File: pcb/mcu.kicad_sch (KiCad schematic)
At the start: 20 parts, among them J4 AVR-UPDI-6, U4 ATtiny1616-MNR

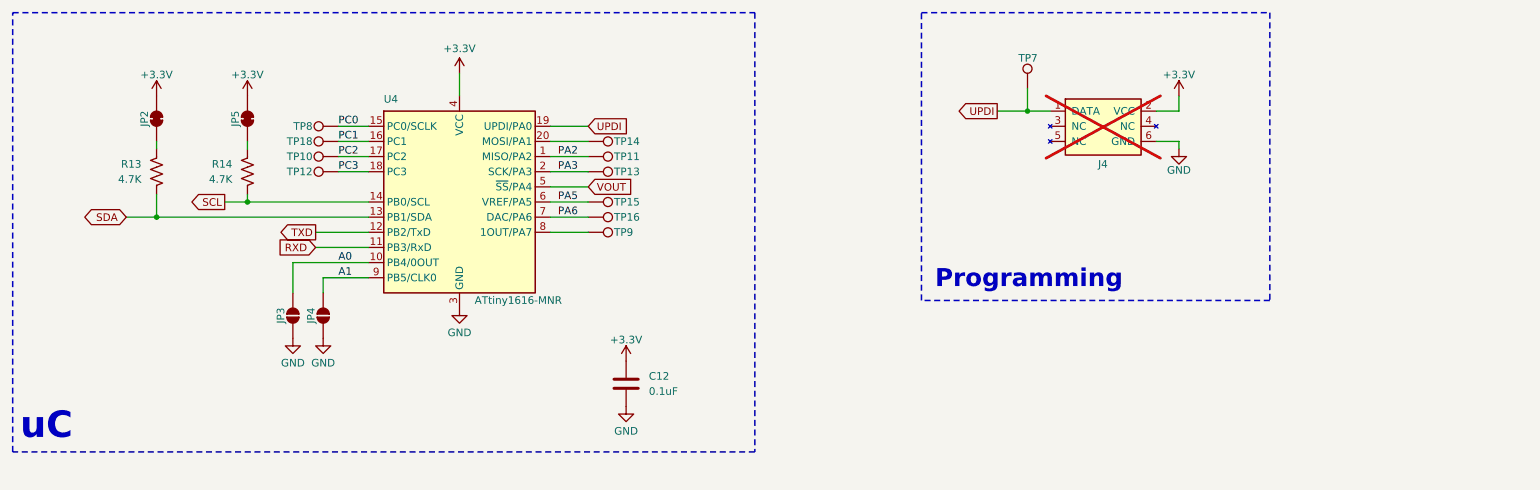
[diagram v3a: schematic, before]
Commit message: Updates for consistency
Changed mounting holes to grounded
Updated power connectors
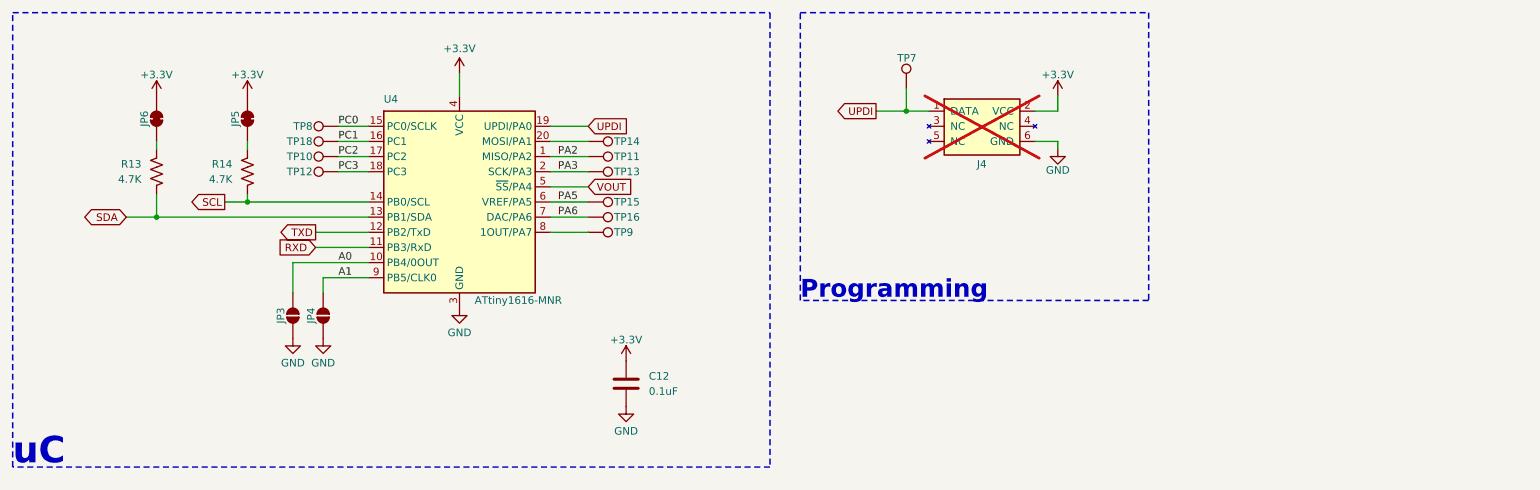
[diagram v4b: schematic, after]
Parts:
- renumbered JP2 to JP6
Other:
- moved on the sheet: J4, TP7
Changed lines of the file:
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@@
 	)
 	(rectangle
-		(start 177.8 25.4)
-		(end 236.22 73.66)
+		(start 157.48 25.4)
+		(end 215.9 73.66)
 		(stroke
 			(width 0.254)
@@
 	(rectangle
 		(start 25.4 25.4)
-		(end 149.86 99.06)
+		(end 152.4 101.6)
 		(stroke
 			(width 0.254)
@@
 	(text "Programming"
 		(exclude_from_sim no)
-		(at 180.086 70.104 0)
+		(at 157.48 73.66 0)
 		(effects
 			(font
@@
 				(bold yes)
 			)
-			(justify left)
+			(justify left bottom)
 		)
 	)
 	(text "uC"
 		(exclude_from_sim no)
-		(at 26.67 94.742 0)
+		(at 25.4 101.6 0)
 		(effects
 			(font
@@
 				(bold yes)
 			)
-			(justify left)
+			(justify left bottom)
 		)
 	)
@@
 	)
 	(junction
-		(at 195.58 41.91)
+		(at 175.26 41.91)
 		(diameter 0)
 		(color 0 0 0 0)
@@
 	(wire
 		(pts
-			(xy 217.17 41.91) (xy 220.98 41.91)
+			(xy 196.85 41.91) (xy 200.66 41.91)
 		)
 		(stroke
@@
 	(wire
 		(pts
-			(xy 220.98 46.99) (xy 220.98 48.26)
+			(xy 200.66 46.99) (xy 200.66 48.26)
 		)
 		(stroke
@@
 	(wire
 		(pts
-			(xy 195.58 41.91) (xy 199.39 41.91)
+			(xy 175.26 41.91) (xy 179.07 41.91)
 		)
 		(stroke
@@
 	(wire
 		(pts
-			(xy 190.5 41.91) (xy 195.58 41.91)
+			(xy 170.18 41.91) (xy 175.26 41.91)
 		)
 		(stroke
@@
 	(wire
 		(pts
-			(xy 195.58 38.1) (xy 195.58 41.91)
+			(xy 175.26 38.1) (xy 175.26 41.91)
 		)
 		(stroke
@@
 	(wire
 		(pts
-			(xy 220.98 39.37) (xy 220.98 41.91)
+			(xy 200.66 39.37) (xy 200.66 41.91)
 		)
 		(stroke
@@
 	(wire
 		(pts
-			(xy 217.17 46.99) (xy 220.98 46.99)
+			(xy 196.85 46.99) (xy 200.66 46.99)
 		)
 		(stroke
@@
 	(global_label "UPDI"
 		(shape output)
-		(at 190.5 41.91 180)
+		(at 170.18 41.91 180)
 		(fields_autoplaced yes)
 		(effects
@@
 		)
 		(property "Intersheetrefs" "${INTERSHEET_REFS}"
-			(at 183.0395 41.91 0)
+			(at 162.7195 41.91 0)
 			(effects
 				(font
@@
 	(symbol
 		(lib_id "CRGM Connector:AVR-UPDI-6")
-		(at 208.28 45.72 0)
+		(at 187.96 45.72 0)
 		(unit 1)
 		(exclude_from_sim no)
@@
 		(dnp yes)
 		(property "Reference" "J4"
-			(at 209.042 50.8 0)
+			(at 188.722 50.8 0)
 			(effects
 				(font
@@
 		)
 		(property "Value" "AVR-UPDI-6"
-			(at 214.122 38.354 0)
+			(at 193.802 38.354 0)
 			(effects
 				(font
@@
 		)
 		(property "Footprint" "CRGM Connector:PinHeader_2x03_P2.54mm_Vertical_SMD"
-			(at 201.93 46.99 90)
+			(at 181.61 46.99 90)
 			(effects
 				(font
@@
 		)
 		(property "Datasheet" "https://www.microchip.com/webdoc/GUID-9D10622A-5C16-4405-B092-1BDD437B4976/index.html?GUID-9B349315-2842-4189-B88C-49F4E1055D7F"
-			(at 208.28 54.102 0)
+			(at 187.96 54.102 0)
 			(effects
 				(font
@@
 		)
 		(property "Description" "Atmel 6-pin UPDI connector"
-			(at 208.28 56.388 0)
+			(at 187.96 56.388 0)
 			(effects
 				(font
@@
 		)
 		(property "LCSC" ""
-			(at 208.28 45.72 0)
+			(at 187.96 45.72 0)
 			(effects
 				(font
@@
 		)
 		(property "Digikey" ""
-			(at 208.28 45.72 0)
+			(at 187.96 45.72 0)
 			(effects
 				(font
@@
 		)
 		(property "Mouser" ""
-			(at 208.28 45.72 0)
+			(at 187.96 45.72 0)
 			(effects
 				(font
@@
 	(symbol
 		(lib_id "CRGM Connector:TestPoint")
-		(at 195.58 38.1 0)
+		(at 175.26 38.1 0)
 		(unit 1)
 		(exclude_from_sim no)
@@
 		(dnp no)
 		(property "Reference" "TP7"
-			(at 194.056 33.02 0)
+			(at 173.736 33.02 0)
 			(effects
 				(font
@@
 		)
 		(property "Value" "~"
-			(at 193.294 33.0199 0)
+			(at 172.974 33.0199 0)
 			(effects
 				(font
@@
 		)
 		(property "Footprint" "CRGM Mechanical:TestPoint_Pad_D1.0mm"
-			(at 195.58 45.466 0)
+			(at 175.26 45.466 0)
 			(effects
 				(font
@@
 		)
 		(property "Datasheet" "~"
-			(at 197.866 36.068 0)
+			(at 177.546 36.068 0)
 			(effects
 				(font
@@
 		)
 		(property "Description" "Test Point D1.0mm"
-			(at 195.58 47.244 0)
+			(at 175.26 47.244 0)
 			(effects
 				(font
@@
 		)
 		(property "LCSC" ""
-			(at 195.58 38.1 0)
+			(at 175.26 38.1 0)
 			(effects
 				(font
@@
 		)
 		(property "Digikey" ""
-			(at 195.58 38.1 0)
+			(at 175.26 38.1 0)
 			(effects
 				(font
@@
 		)
 		(property "Mouser" ""
-			(at 195.58 38.1 0)
+			(at 175.26 38.1 0)
 			(effects
 				(font
@@
 		(on_board yes)
 		(dnp no)
-		(property "Reference" "JP2"
+		(property "Reference" "JP6"
 			(at 47.498 43.18 0)
 			(effects
@@
 			(project "current-module"
 				(path "/a8149920-3b7f-4d7d-8e96-7a0b38870225/573c51ea-89ab-4745-b6d8-c69e780cd603"
-					(reference "JP2")
+					(reference "JP6")
 					(unit 1)
 				)
@@
 	(symbol
 		(lib_id "power:GND")
-		(at 220.98 48.26 0)
+		(at 200.66 48.26 0)
 		(unit 1)
 		(exclude_from_sim no)
@@
 		(dnp no)
 		(property "Reference" "#PWR0108"
-			(at 220.98 54.61 0)
+			(at 200.66 54.61 0)
 			(effects
 				(font
@@
 		)
 		(property "Value" "GND"
-			(at 220.98 51.816 0)
+			(at 200.66 51.816 0)
 			(effects
 				(font
@@
 		)
 		(property "Footprint" ""
-			(at 220.98 48.26 0)
+			(at 200.66 48.26 0)
 			(effects
 				(font
@@
 		)
 		(property "Datasheet" ""
-			(at 220.98 48.26 0)
+			(at 200.66 48.26 0)
 			(effects
 				(font
@@
 		)
 		(property "Description" "Power symbol creates a global label with name \"GND\" , ground"
-			(at 220.98 48.26 0)
+			(at 200.66 48.26 0)
 			(effects
 				(font
@@
 	(symbol
 		(lib_id "power:+3.3V")
-		(at 220.98 39.37 0)
+		(at 200.66 39.37 0)
 		(unit 1)
 		(exclude_from_sim no)
@@
 		(dnp no)
 		(property "Reference" "#PWR0109"
-			(at 220.98 43.18 0)
+			(at 200.66 43.18 0)
 			(effects
 				(font
@@
 		)
 		(property "Value" "+3.3V"
-			(at 220.98 35.814 0)
+			(at 200.66 35.814 0)
 			(effects
 				(font
@@
 		)
 		(property "Footprint" ""
-			(at 220.98 39.37 0)
+			(at 200.66 39.37 0)
 			(effects
 				(font
@@
 		)
 		(property "Datasheet" ""
-			(at 220.98 39.37 0)
+			(at 200.66 39.37 0)
 			(effects
 				(font
@@
 		)
 		(property "Description" "Power symbol creates a global label with name \"+3.3V\""
-			(at 220.98 39.37 0)
+			(at 200.66 39.37 0)
 			(effects
 				(font

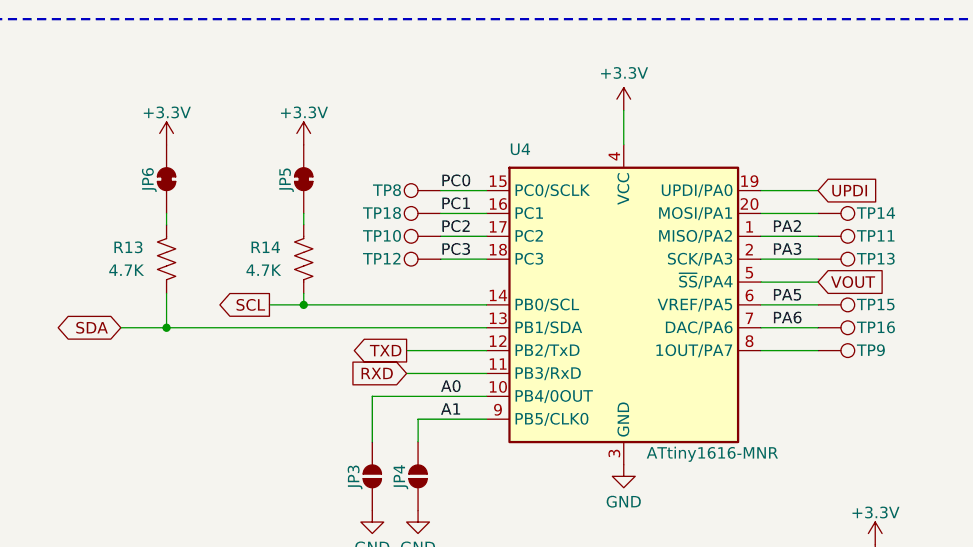
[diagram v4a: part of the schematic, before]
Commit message: Removed power connectors
Removed power connector as 5v is not necessary.
Added 100uF caps to power
Added TVS to I2C and VOUT
Rerouted entire board
Adjusted silkscreen
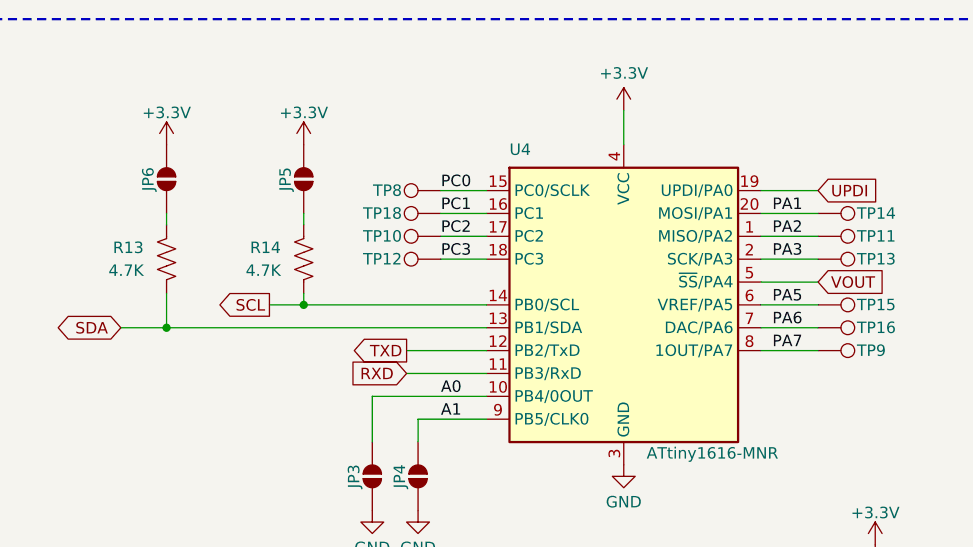
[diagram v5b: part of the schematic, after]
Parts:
- JP5, JP6: footprint CRGM Connector:SolderJumper-2_P1.3mm_Bridged_RoundedPad1.0x1.5mm -> CRGM Connector:SolderJumper-2_P1.3mm_Open_RoundedPad1.0x1.5mm; symbol Jumper:SolderJumper_2_Bridged -> CRGM Connector:SolderJumper_2_Open
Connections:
- net PA7: now reaches TP9.1, U4.8 (1OUT/PA7)
- net PA1: now reaches TP14.1, U4.20 (MOSI/PA1)
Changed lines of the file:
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@@
+		)
+	)
+	(label "PA7"
+		(at 116.84 62.23 0)
+		(effects
+			(font
+				(size 1.27 1.27)
+			)
+			(justify left bottom)
 		)
 	)
@@
 	(label "PA3"
 		(at 116.84 52.07 0)
+		(effects
+			(font
+				(size 1.27 1.27)
+			)
+			(justify left bottom)
+		)
+	)
+	(label "PA1"
+		(at 116.84 46.99 0)
 		(effects
 			(font
@@
 	)
 	(symbol
-		(lib_id "Jumper:SolderJumper_2_Bridged")
+		(lib_id "CRGM Connector:SolderJumper_2_Open")
 		(at 64.77 43.18 90)
 		(unit 1)
@@
 			)
 		)
-		(property "Footprint" "CRGM Connector:SolderJumper-2_P1.3mm_Bridged_RoundedPad1.0x1.5mm"
-			(at 64.77 43.18 0)
+		(property "Footprint" "CRGM Connector:SolderJumper-2_P1.3mm_Open_RoundedPad1.0x1.5mm"
+			(at 75.184 43.18 0)
 			(effects
 				(font
@@
 		)
 		(property "Datasheet" "~"
-			(at 64.77 43.18 0)
-			(effects
-				(font
-					(size 1.27 1.27)
-				)
-				(hide yes)
-			)
-		)
-		(property "Description" "Solder Jumper, 2-pole, closed/bridged"
-			(at 64.77 43.18 0)
+			(at 72.898 43.18 0)
+			(effects
+				(font
+					(size 1.27 1.27)
+				)
+				(hide yes)
+			)
+		)
+		(property "Description" "Solder Jumper, 2-pole, open"
+			(at 70.104 43.18 0)
 			(effects
 				(font
@@
 	)
 	(symbol
-		(lib_id "Jumper:SolderJumper_2_Bridged")
+		(lib_id "CRGM Connector:SolderJumper_2_Open")
 		(at 49.53 43.18 90)
 		(unit 1)
@@
 			)
 		)
-		(property "Footprint" "CRGM Connector:SolderJumper-2_P1.3mm_Bridged_RoundedPad1.0x1.5mm"
-			(at 49.53 43.18 0)
+		(property "Footprint" "CRGM Connector:SolderJumper-2_P1.3mm_Open_RoundedPad1.0x1.5mm"
+			(at 59.944 43.18 0)
 			(effects
 				(font
@@
 		)
 		(property "Datasheet" "~"
-			(at 49.53 43.18 0)
-			(effects
-				(font
-					(size 1.27 1.27)
-				)
-				(hide yes)
-			)
-		)
-		(property "Description" "Solder Jumper, 2-pole, closed/bridged"
-			(at 49.53 43.18 0)
-			(effects
-				(font
+			(at 57.658 43.18 0)
+			(effects
+				(font
+					(size 1.27 1.27)
+				)
+				(hide yes)
+			)
+		)
+		(property "Description" "Solder Jumper, 2-pole, open"
+			(at 54.864 43.18 0)
+			(effects
+				(font

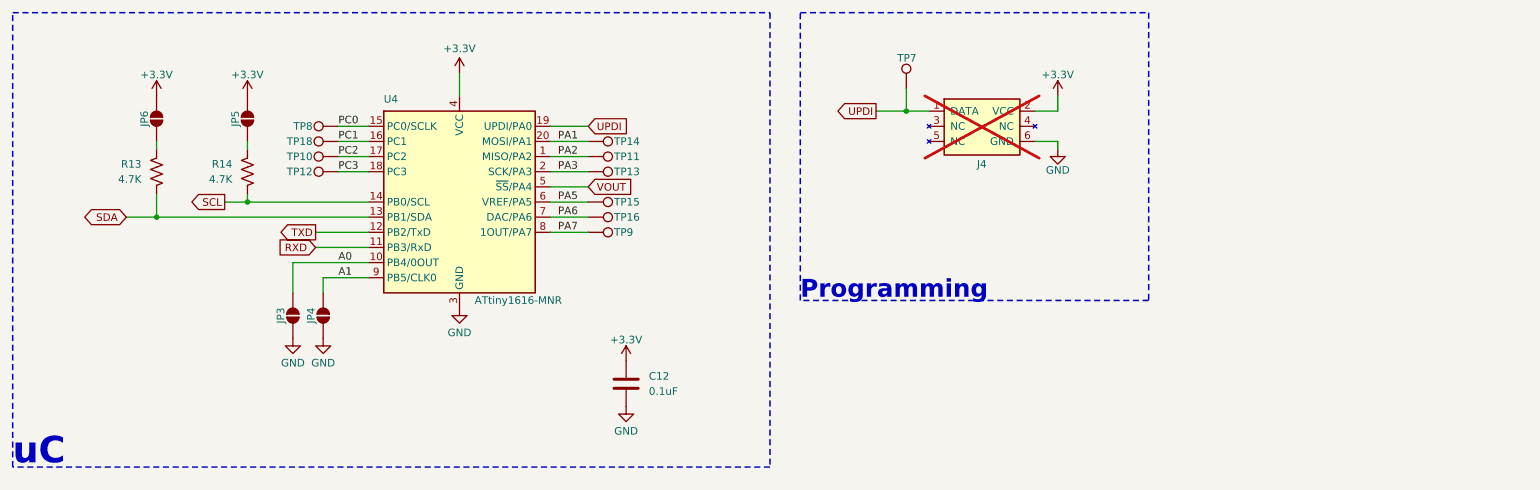
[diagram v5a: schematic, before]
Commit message: Collapsed UPDI and Serial
Added indicator LEDs
Rerouted
Cleaned up silkscreen
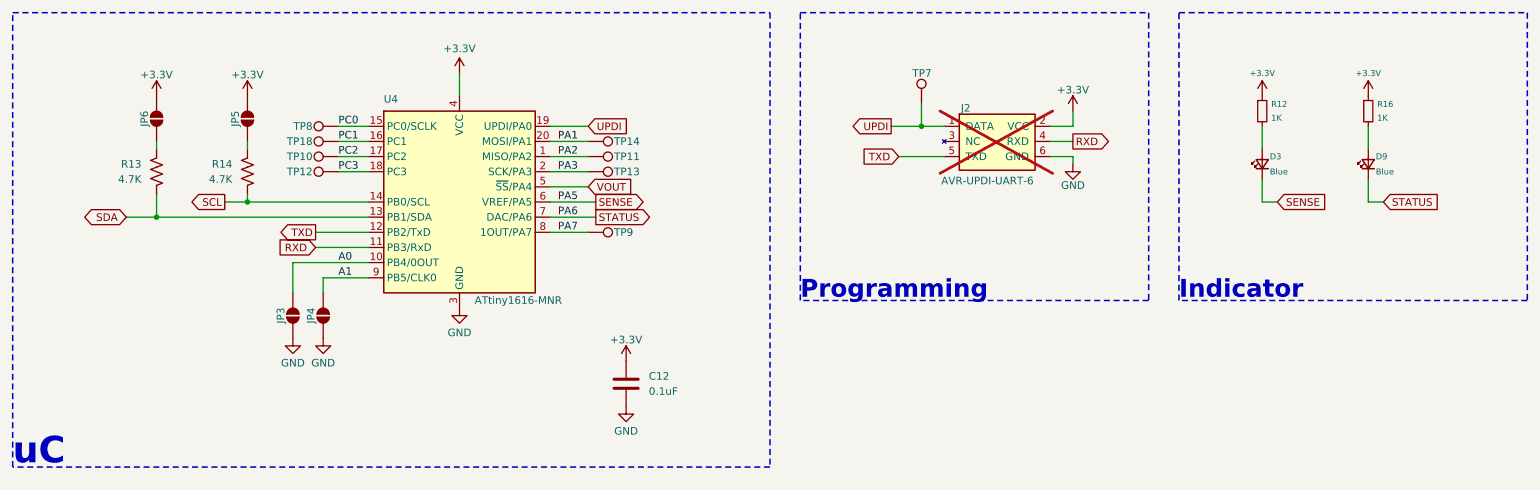
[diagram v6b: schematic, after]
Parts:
- removed J4: AVR-UPDI-6, CRGM Connector:PinHeader_2x03_P2.54mm_Vertical_SMD, symbol CRGM Connector:AVR-UPDI-6
- removed TP15, TP16: ~, CRGM Mechanical:TestPoint_Pad_D1.0mm, symbol CRGM Connector:TestPoint
- added D3, D9: Blue, CRGM Passive:LED_0603_1608Metric, symbol Device:LED_Small
- added J2: AVR-UPDI-UART-6, CRGM Connector:PinHeader_2x03_P2.54mm_Vertical_SMD, symbol CRGM Connector:AVR-UPDI-UART-6
- added R12, R16: 1K, CRGM Passive:R_0603_1608Metric, symbol Device:R_Small
- U4: footprint CRG Makes:VQFN-20-1EP_3x3mm_P0.4mm_EP1.7x1.7mm_ThermalVias -> Package_DFN_QFN:VQFN-20-1EP_3x3mm_P0.4mm_EP1.7x1.7mm
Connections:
- net +3.3V: now also J2.2 (VCC), R12.1, R16.1
- net GND: now also J2.6 (GND)
- net RXD: now also J2.4 (RXD)
- net TXD: now also J2.5 (TXD)
- net UPDI: now also J2.1 (DATA)
- net PA5 renamed SENSE
- net SENSE: now also D3.1 (K)
- net PA6 renamed STATUS
- net STATUS: now also D9.1 (K)
- new net: D3.2 (A), R12.2
- new net: D9.2 (A), R16.2
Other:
- note added: "Indicator"
- moved on the sheet: TP7
